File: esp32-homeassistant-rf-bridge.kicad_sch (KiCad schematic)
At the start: 35 parts, among them J1 USB_C_Receptacle_USB2.0_16P, J2 Conn_02x04_Odd_Even, SW1 SW_Push, SW2 SW_Push, SW3 SW_Push, SW4 SW_Push, U1 ESP32-S2-MINI-1, U2 TSOP41xx, U3 XC6206P332MR, U4 CC1101_E07-M1101D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

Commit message: silkscreen updates, add LDR and mounting holes
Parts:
- added R5: LDR07, OptoDevice:R_LDR_5.0x4.1mm_P3mm_Vertical, symbol Sensor_Optical:LDR07
- added R6: 10K, Resistor_SMD:R_0402_1005Metric, symbol Device:R
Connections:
- net +3.3V: now also R5.1
- net GND: now also R6.2
- net LDR: now reaches U1.32 (GPIO36)
- net LDR: now also R5.2, R6.1
- no-connect marks 21 -> 20
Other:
- note added: "PHOTORESISTOR"

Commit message: update production files
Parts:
- R5: now left out of the parts list
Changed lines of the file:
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@@
 		(unit 1)
 		(exclude_from_sim no)
-		(in_bom yes)
+		(in_bom no)
 		(on_board yes)
 		(dnp no)

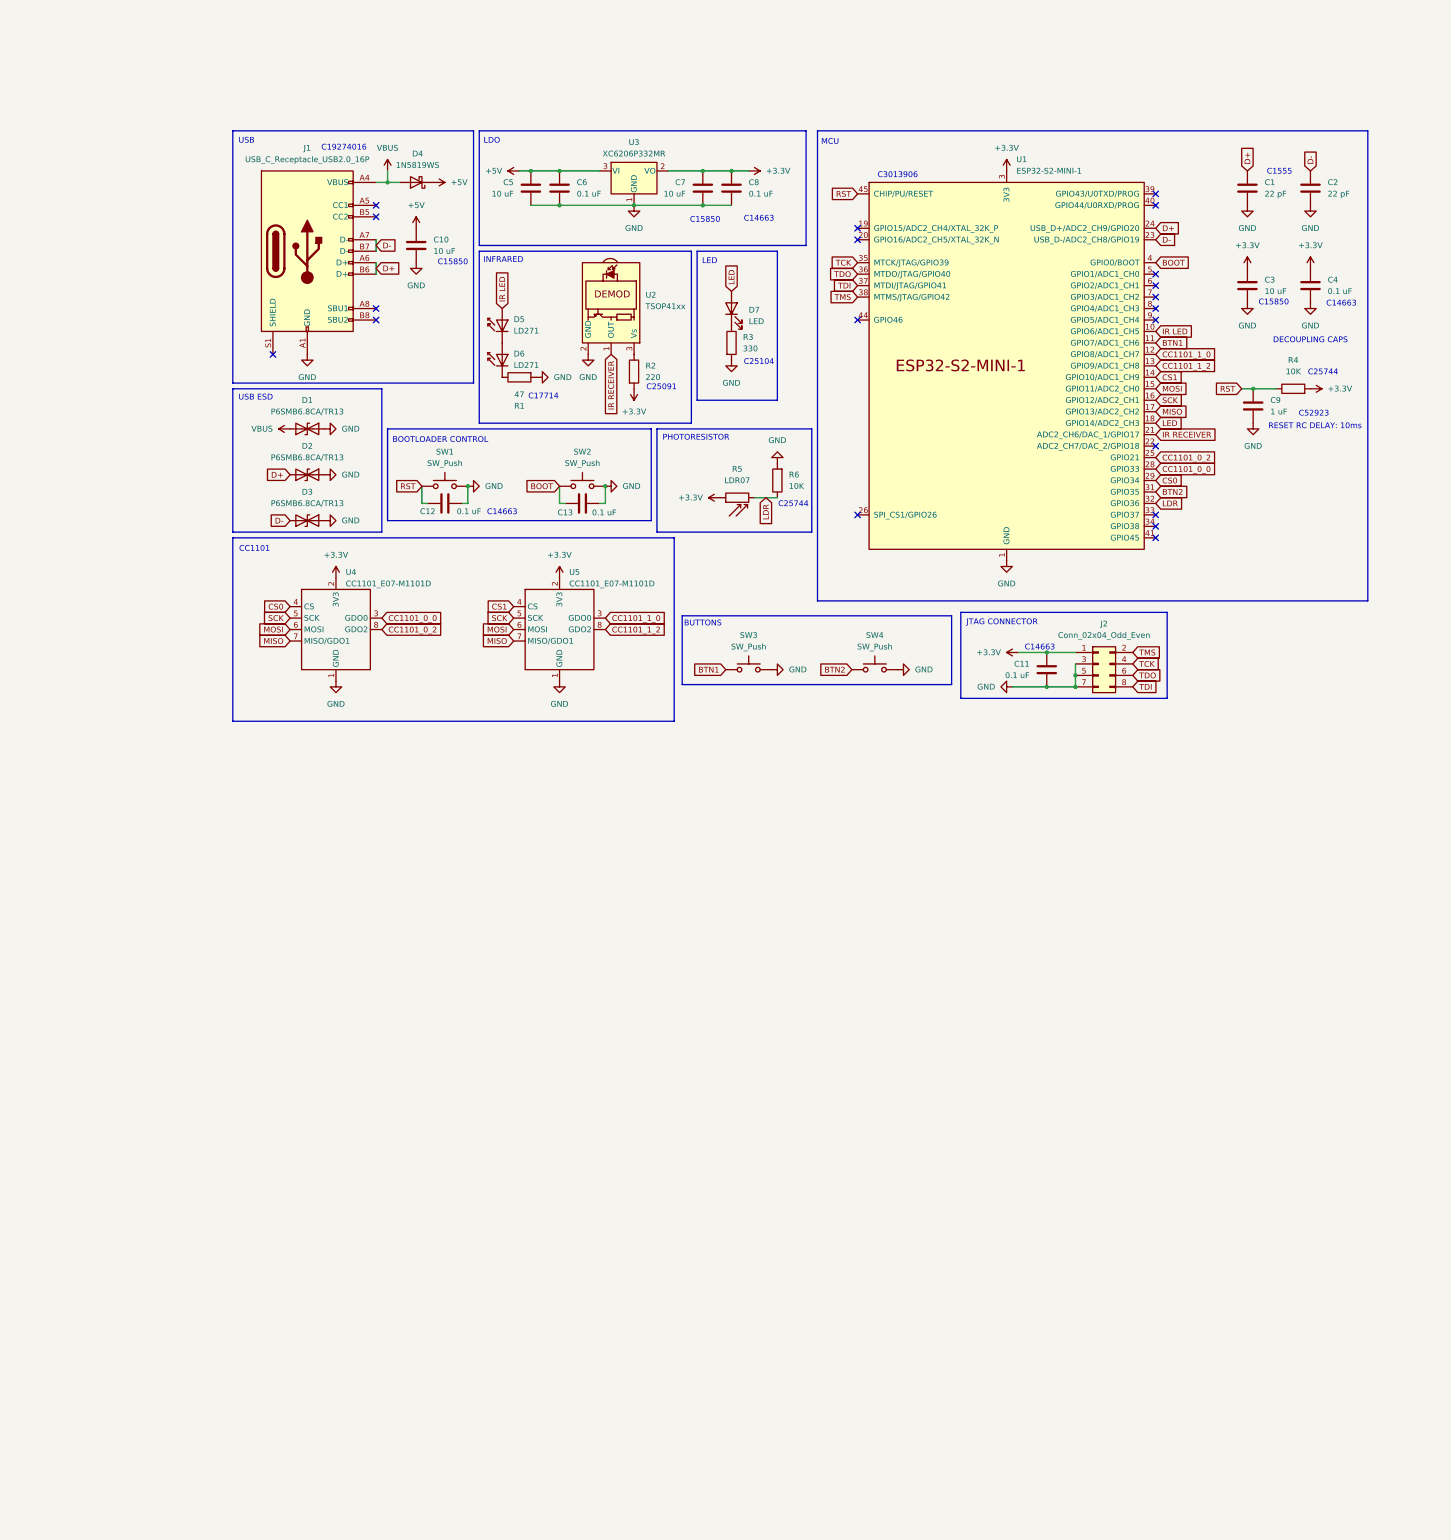
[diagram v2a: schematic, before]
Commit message: make board smaller, remove problematic components
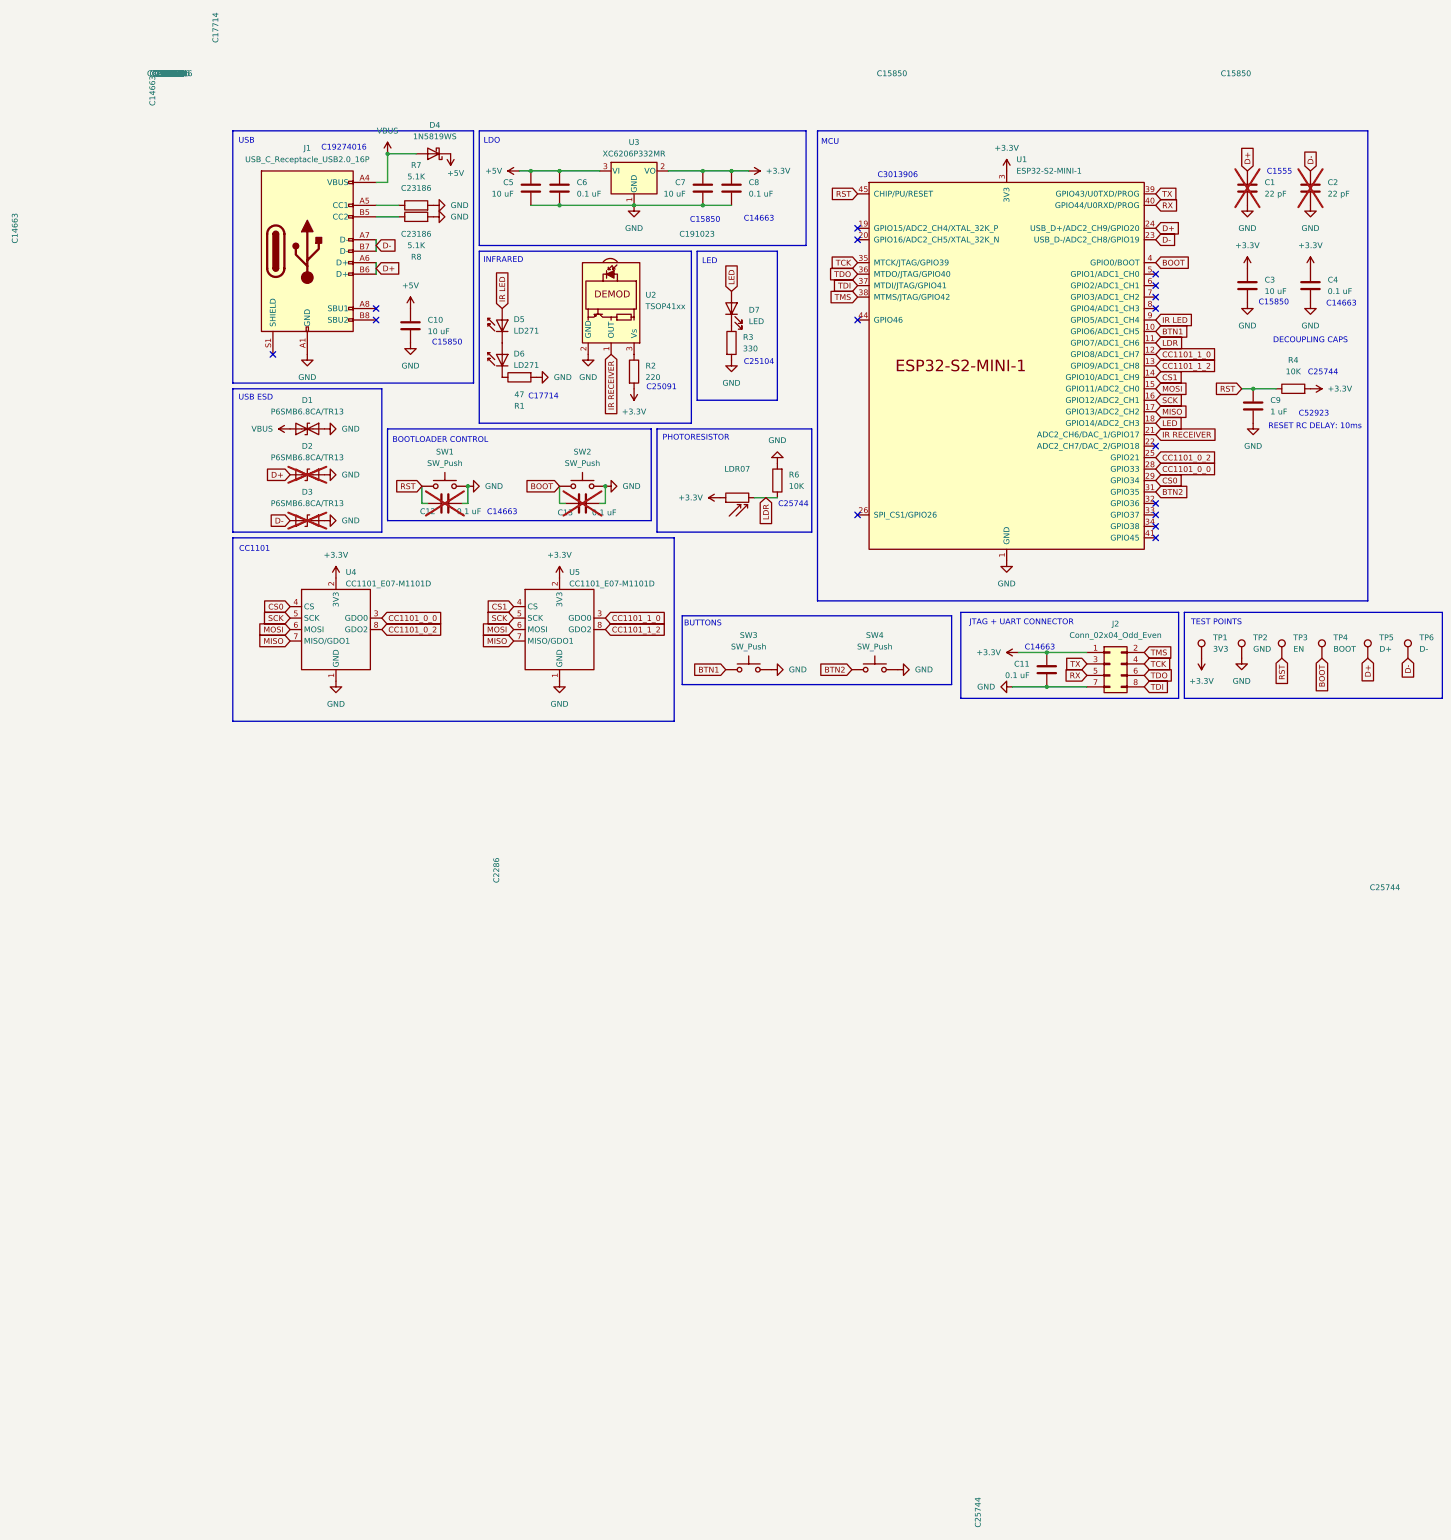
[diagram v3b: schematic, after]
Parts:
- added R7, R8: 5.1K, Resistor_SMD:R_0603_1608Metric, symbol Device:R
- added TP1: 3V3, TestPoint:TestPoint_Pad_D3.0mm, symbol Connector:TestPoint
- added TP2: GND, TestPoint:TestPoint_Pad_D3.0mm, symbol Connector:TestPoint
- added TP3: EN, TestPoint:TestPoint_Pad_D3.0mm, symbol Connector:TestPoint
- added TP4: BOOT, TestPoint:TestPoint_Pad_D3.0mm, symbol Connector:TestPoint
- added TP5: D+, TestPoint:TestPoint_Pad_D3.0mm, symbol Connector:TestPoint
- added TP6: D-, TestPoint:TestPoint_Pad_D3.0mm, symbol Connector:TestPoint
- C1, C2: LCSC (none) -> C1555; now not fitted
- C10, C3, C5, C7: LCSC (none) -> C15850
- C11, C4, C6, C8: LCSC (none) -> C14663
- C12, C13: LCSC (none) -> C14663; now not fitted
- C9: LCSC (none) -> C52923
- D1: LCSC (none) -> C78395
- D2, D3: LCSC (none) -> C78395; now not fitted
- D4: LCSC (none) -> C191023
- D7: LCSC (none) -> C2286
- J1: LCSC (none) -> C19274016
- LDR07: renamed from R5; value LDR07 -> ~
- R1: LCSC (none) -> C17714
- R2: LCSC (none) -> C25091
- R3: LCSC (none) -> C25104
- R4, R6: LCSC (none) -> C25744
- SW1, SW2: LCSC (none) -> C318884
- SW3, SW4: footprint Button_Switch_THT:SW_PUSH-12mm -> Button_Switch_THT:SW_PUSH_6mm
- U1: LCSC (none) -> C3013906
- U3: LCSC (none) -> C5446
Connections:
- net +3.3V: now also TP1.1
- net BOOT: now also TP4.1
- net BTN1: now also U1.10 (GPIO6/ADC1_CH5); no longer U1.11 (GPIO7/ADC1_CH6)
- net D+: now also TP5.1
- net D-: now also TP6.1
- net GND: now also R7.2, R8.2, TP2.1; no longer J2.3 (Pin_3), J2.5 (Pin_5)
- net IR LED: now also U1.9 (GPIO5/ADC1_CH4); no longer U1.10 (GPIO6/ADC1_CH5)
- net LDR: now also U1.11 (GPIO7/ADC1_CH6); no longer U1.32 (GPIO36)
- net RST: now also TP3.1
- net at J1.A5 (CC1): now also R7.1
- net at J1.B5 (CC2): now also R8.1
- net TX: now reaches U1.39 (GPIO43/U0TXD/PROG)
- net TX: now also J2.3 (Pin_3)
- net RX: now reaches U1.40 (GPIO44/U0RXD/PROG)
- net RX: now also J2.5 (Pin_5)
- no-connect marks 20 -> 16
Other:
- note added: "JTAG + UART CONNECTOR"
- note added: "TEST POINTS"
- note removed: "JTAG CONNECTOR"
- moved on the sheet: C10, D4, J2

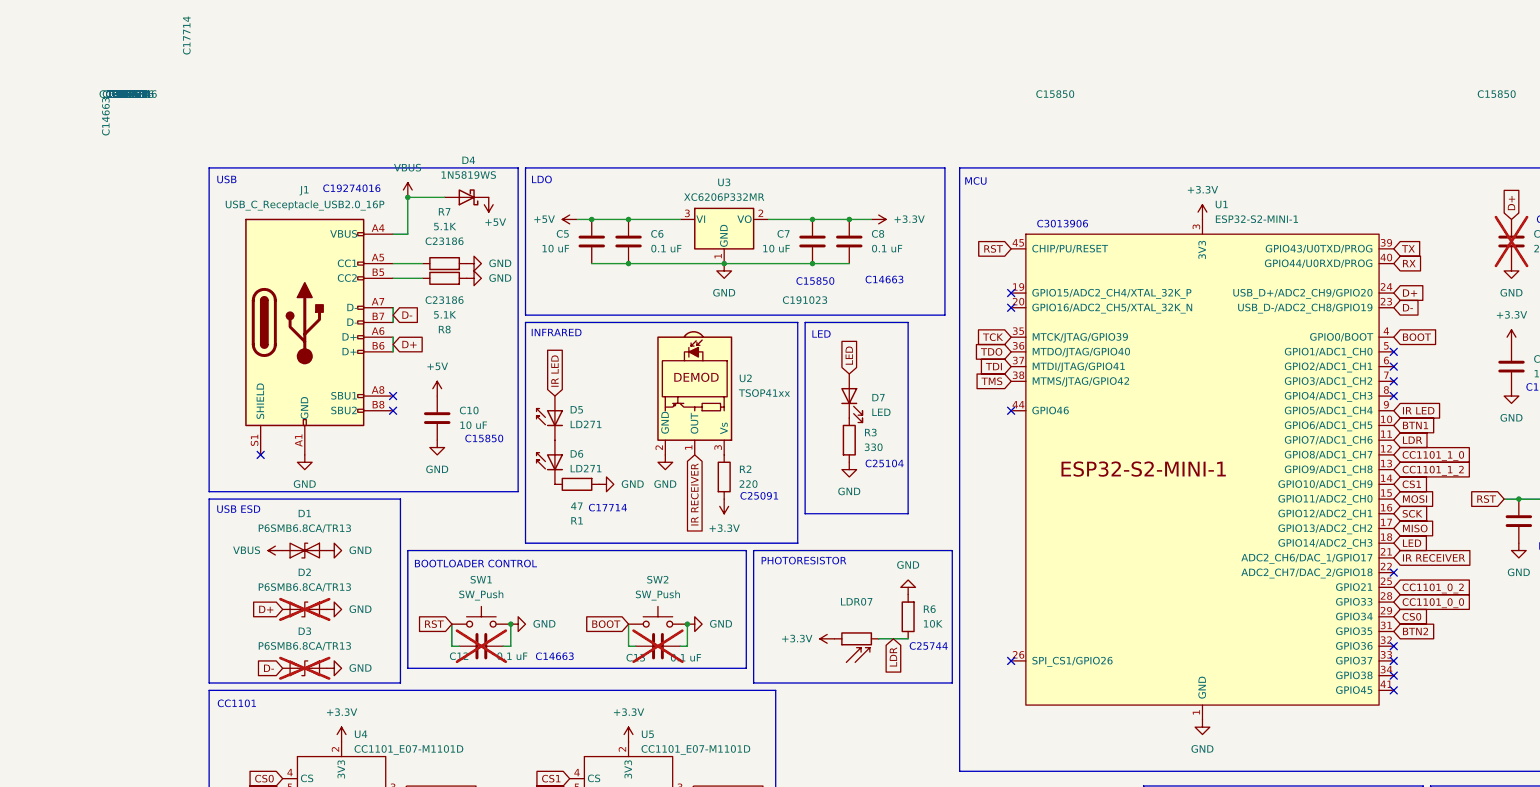
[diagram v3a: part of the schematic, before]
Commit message: use ams1117
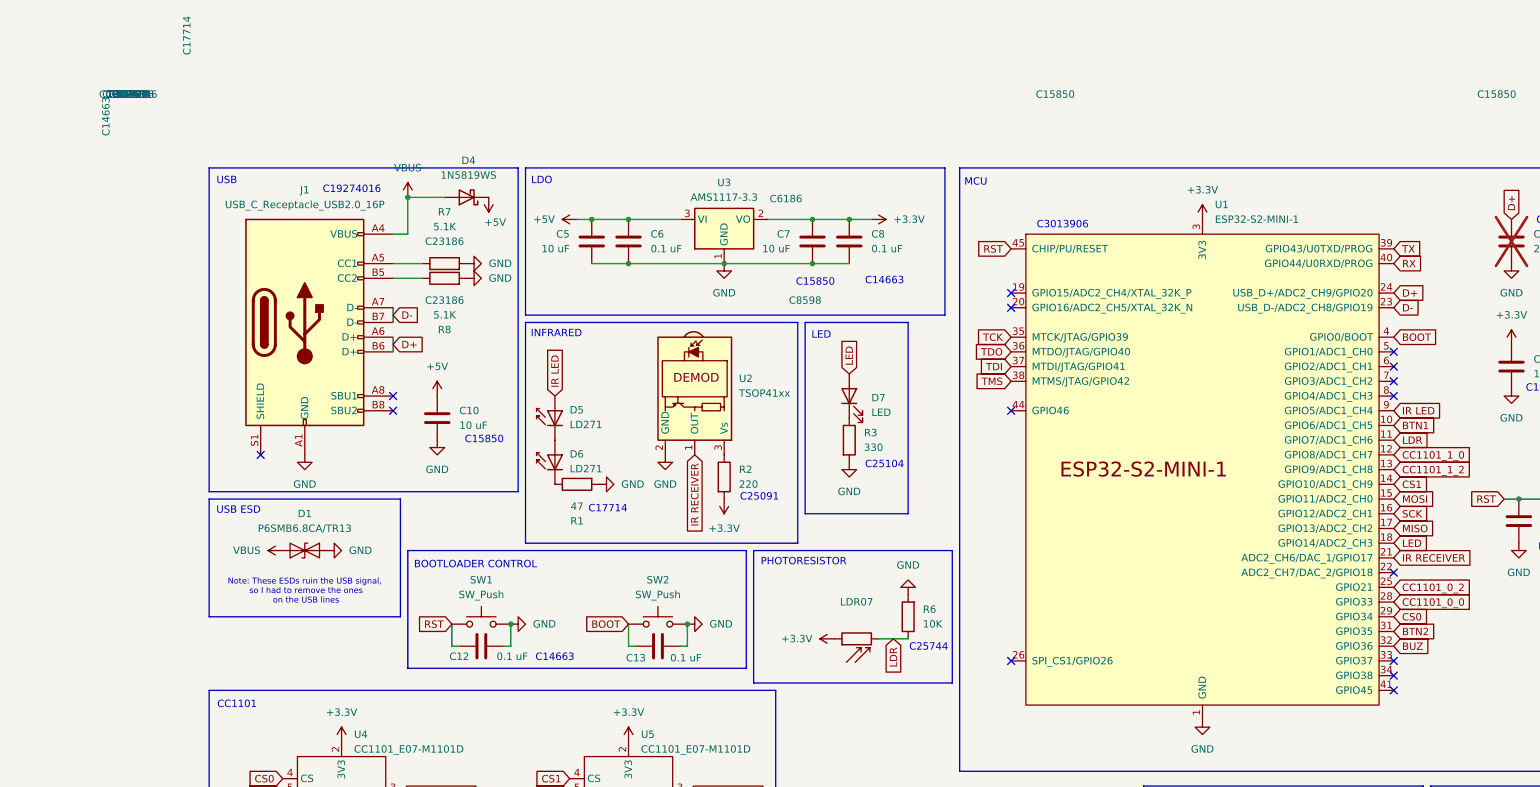
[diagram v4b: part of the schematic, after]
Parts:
- removed D2, D3: P6SMB6.8CA/TR13, Diode_SMD:D_SMB, symbol Diode:ESD9B3.3ST5G
- removed U3: XC6206P332MR, Package_TO_SOT_SMD:SOT-23-3, symbol Regulator_Linear:XC6206PxxxMR
- added U3: AMS1117-3.3, Package_TO_SOT_SMD:SOT-223-3_TabPin2, symbol Regulator_Linear:AMS1117-3.3
- C12, C13: now fitted
- D4: footprint Diode_SMD:D_SOD-323 -> Diode_SMD:D_SOD-123; LCSC C191023 -> C8598
- TP1, TP2, TP3, TP4, TP5, TP6: now left out of the parts list
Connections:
- net +3.3V: now also U3.2 (VO)
- net +5V: now also U3.3 (VI)
- net GND: now also U3.1 (GND)
- net BUZ: now reaches U1.32 (GPIO36)
- no-connect marks 16 -> 15
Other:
- note added: "Note: These ESDs ruin the USB signal, so I had to remove the ones on the USB lines"
